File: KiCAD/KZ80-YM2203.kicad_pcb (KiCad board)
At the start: 2 copper layers, 100 x 75 mm, 38 parts, among them J1 SBC8080 BUS, J2 AD-JP1, J3 AD-JP1, J4 Audio-Jack, J5 A-CON, J6 B-CON, U1 NJM5532DD, U2 74LS139, U3 74HCU04, U4 YM2203, U5 YM3014B, Y1 3.579545MHz

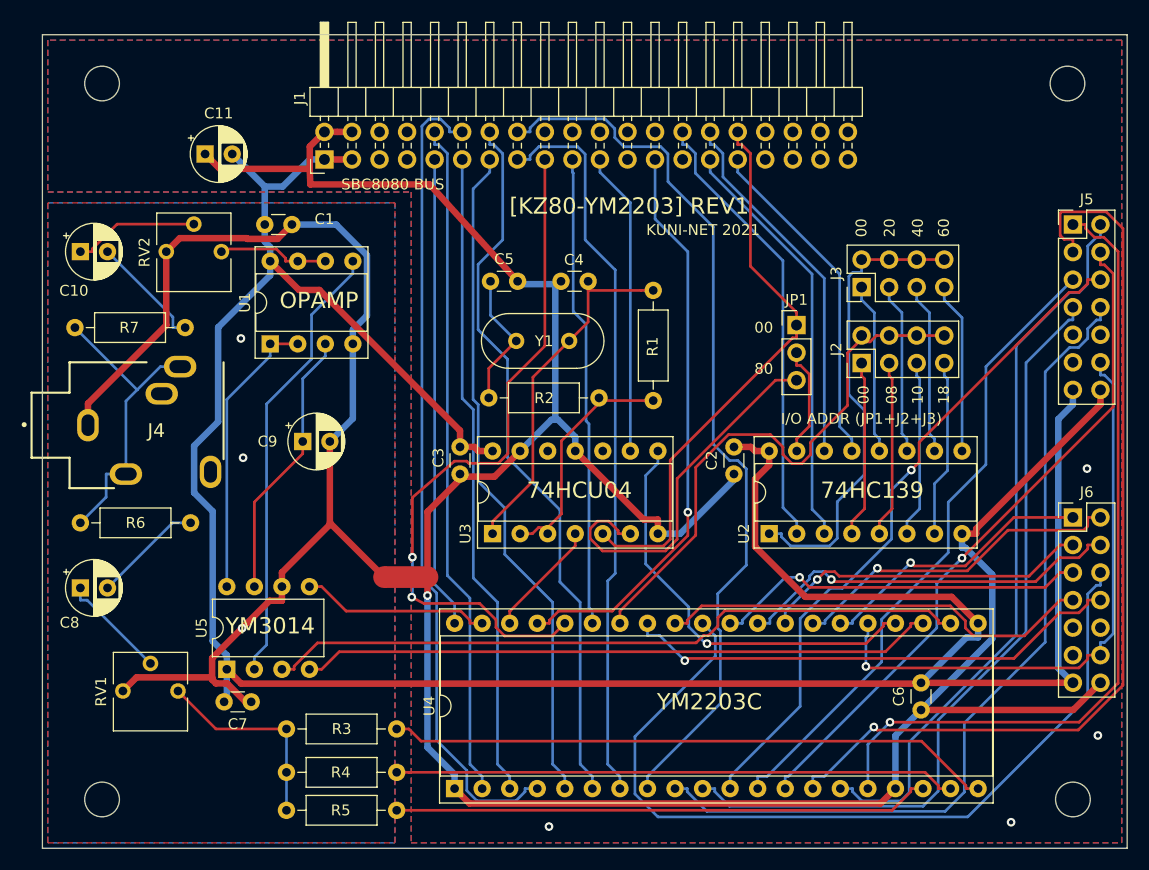
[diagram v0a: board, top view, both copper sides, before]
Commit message: パターンを基板縁から離す対応を実施・ガーバー出力
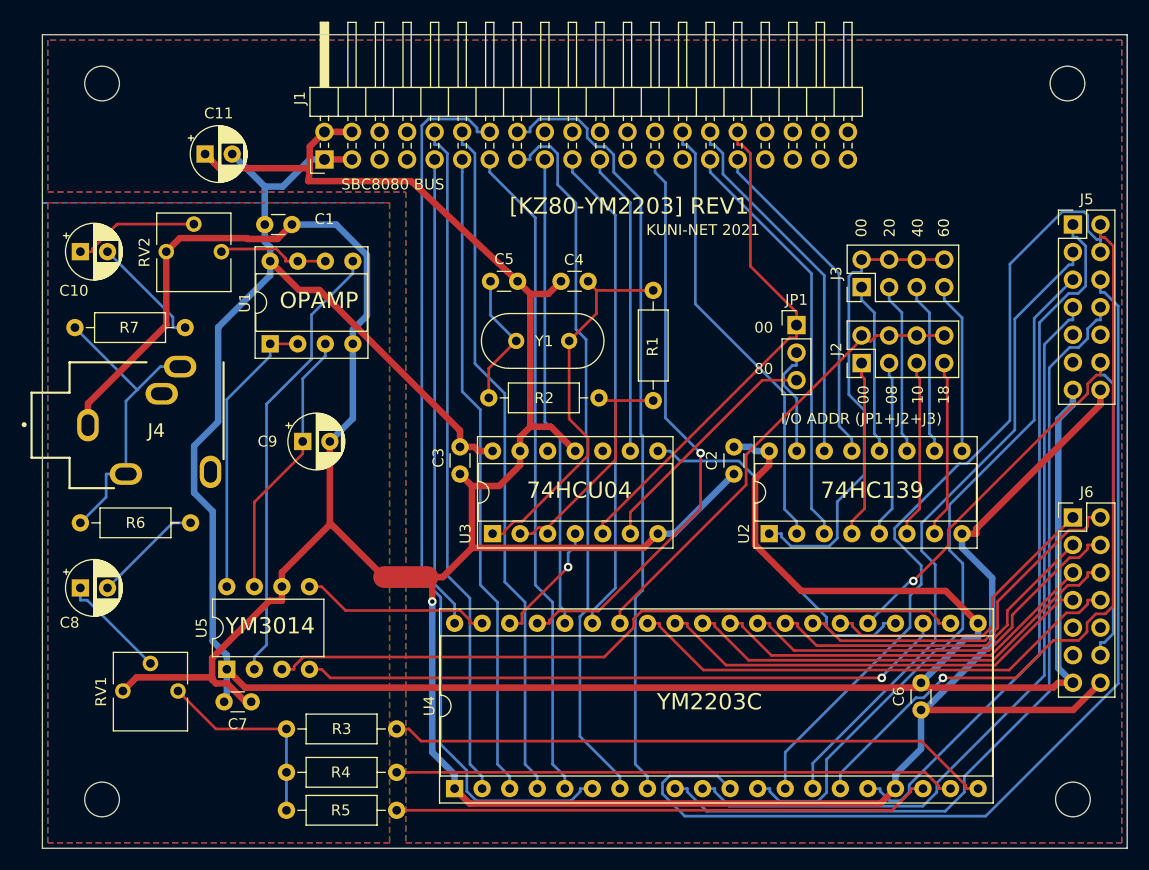
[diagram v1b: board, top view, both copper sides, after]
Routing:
- net /IOB5: track 78.7 -> 41.8 mm
- net /IOA5: track 62.9 -> 94.0 mm, vias 1 -> 0
- net /IOA2: track 86.6 -> 60.6 mm, vias 1 -> 0
- net /~IORD: track 64.6 -> 43.5 mm, vias 2 -> 0
- net /D5: track 66.6 -> 82.9 mm
- net Net-(JP1-Pad3): track 34.8 -> 22.3 mm
- net /D3: track 75.2 -> 63.6 mm
- net /D7: track 82.3 -> 71.7 mm
- net /IOA3: track 62.9 -> 72.8 mm, vias 1 -> 0
- net /IOA0: track 74.7 -> 65.0 mm, vias 1 -> 0
- net Net-(J2-Pad2): track 51.9 -> 43.7 mm
- net /~IRQ: track 54.8 -> 61.9 mm
- net GND: track 232.3 -> 239.3 mm, vias 5 -> 1
- net /IOA4: track 59.5 -> 65.3 mm
- net /~RES: track 39.0 -> 33.8 mm, vias 1 -> 0
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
